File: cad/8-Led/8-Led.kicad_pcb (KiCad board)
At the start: 2 copper layers, 31.8 x 50.8 mm, 21 parts, among them J1 Screw_Terminal_01x02

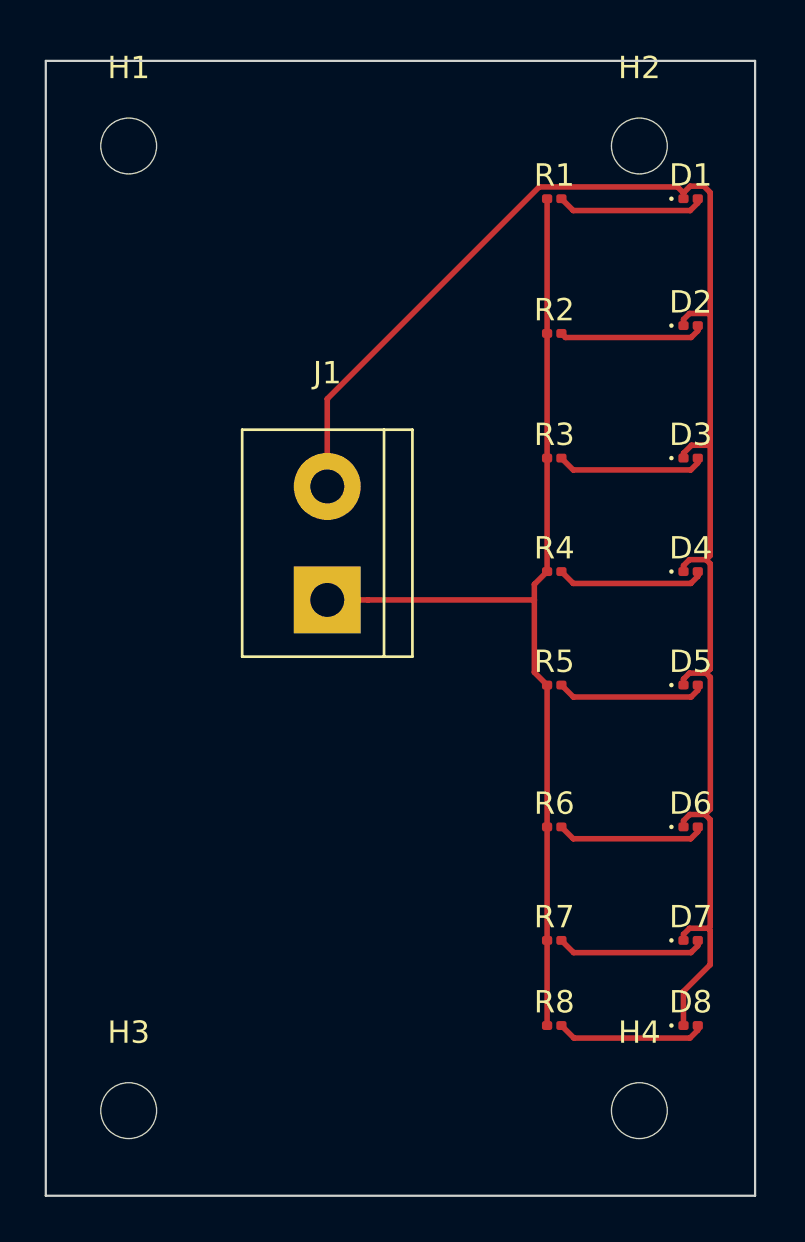
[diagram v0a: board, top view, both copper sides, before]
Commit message: kicad 8Led reduced board size
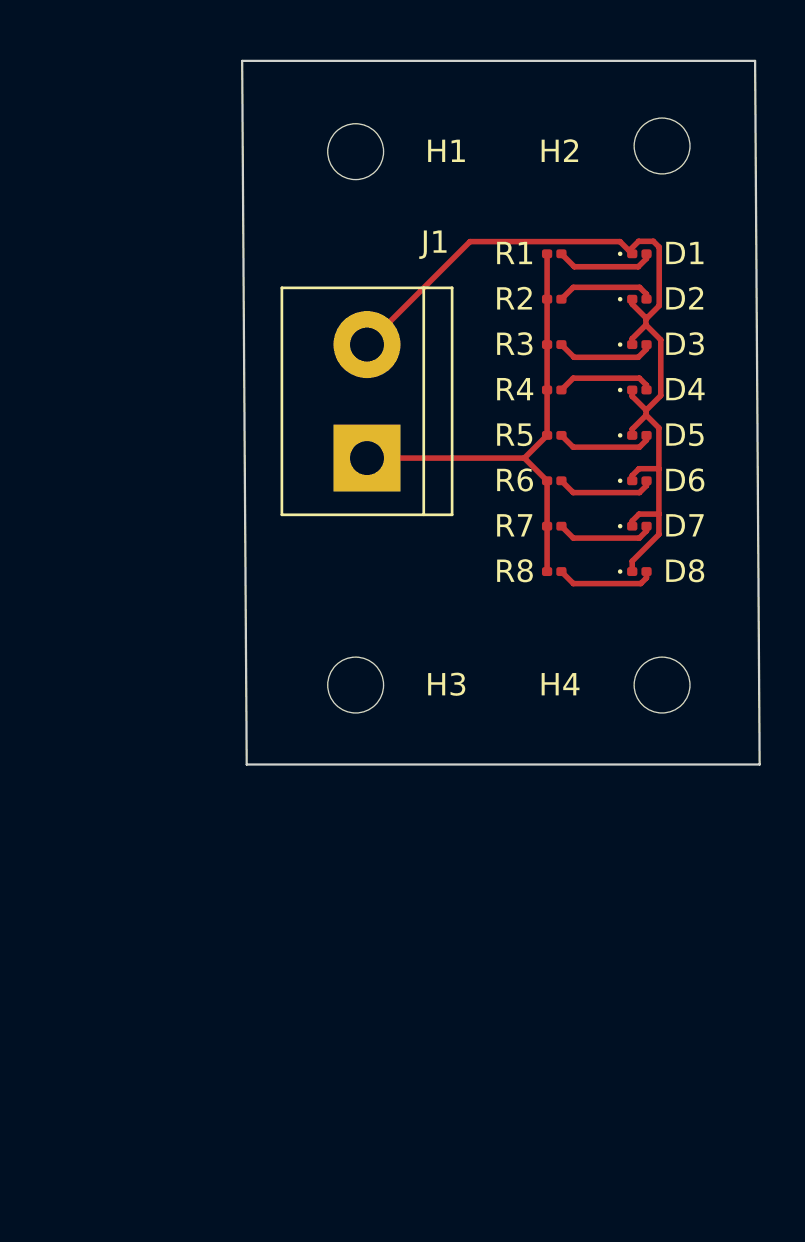
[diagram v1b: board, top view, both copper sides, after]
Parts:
- moved H3 21.6 mm to (99.1, 149.9)
- moved D8 20.4 mm to (111.8, 144.8)
- moved R8 20.3 mm to (108.0, 144.8)
- moved H4 19.1 mm to (112.8, 149.9)
- moved D7 18.7 mm to (111.8, 142.7)
- moved R7 18.5 mm to (108.0, 142.7)
- moved D6 15.7 mm to (111.8, 140.7)
- moved R6 15.5 mm to (108.0, 140.7)
- moved D5 11.4 mm to (111.8, 138.7)
- moved R5 11.2 mm to (108.0, 138.7)
- moved H1 10.2 mm to (99.1, 126.0)
- moved D4 8.45 mm to (111.8, 136.7)
- moved R4 8.13 mm to (108.0, 136.7)
- moved J1 6.59 mm to (99.6, 139.7)
- moved D3 5.57 mm to (111.8, 134.6)
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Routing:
- net GND: track 72.7 -> 39.4 mm
- net VCC: track 46.8 -> 22.1 mm
- net Net-(D7-Pad2): track 6.70 -> 4.38 mm
- net Net-(D5-Pad2): track 6.69 -> 4.37 mm
- net Net-(D4-Pad2): track 6.67 -> 4.37 mm
- net Net-(D6-Pad2): track 6.67 -> 4.38 mm
- net Net-(D3-Pad2): track 6.67 -> 4.40 mm
- net Net-(D8-Pad2): track 6.69 -> 4.42 mm
- net Net-(D1-Pad2): track 6.66 -> 4.41 mm
- net Net-(D2-Pad2): track 6.54 -> 4.38 mm
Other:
- board size 31.8 x 50.8 mm -> 23.2 x 31.5 mm
